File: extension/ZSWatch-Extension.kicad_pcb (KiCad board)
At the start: 4 copper layers, 16.8 x 16.8 mm, 37 parts, among them IC501 MAX32664, IC502 LIS2DS12, IC503 MAX86141, IC601 DA7212-01UM2, X701 MB2, X702 MB1, Y501 32kHz

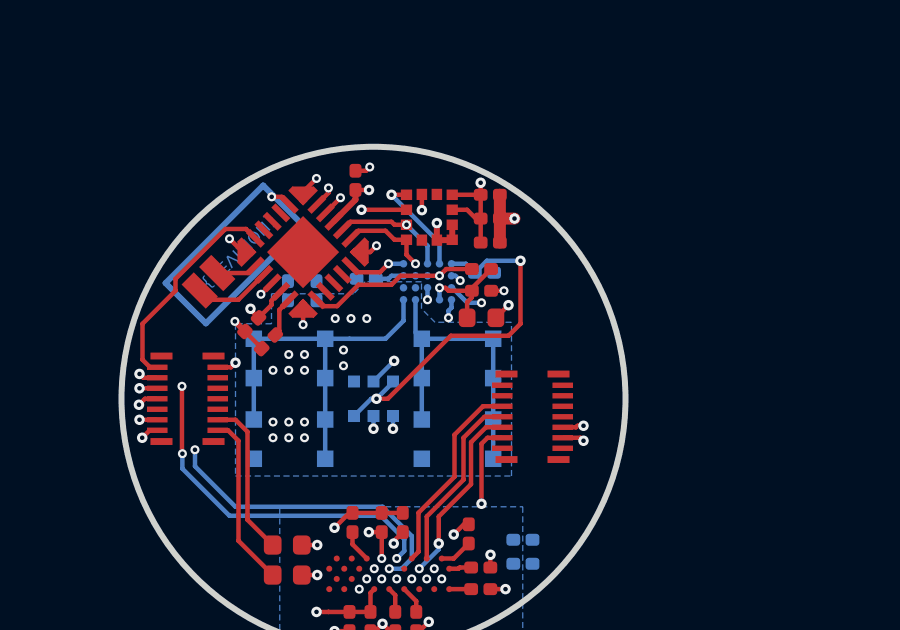
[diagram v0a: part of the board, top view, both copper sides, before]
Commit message: Bug: Issue #3
- Replace VLED capacitor with 10 V type

Closes: #3

Signed-off-by: Daniel Kampert <DanielKampert@kampis-elektroecke.de>
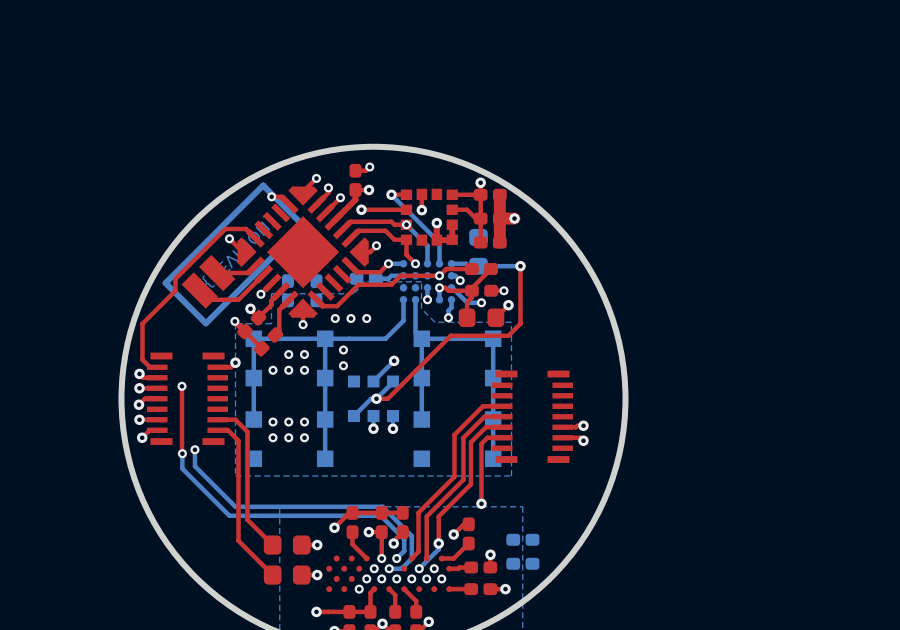
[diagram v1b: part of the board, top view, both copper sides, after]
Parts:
- C508: footprint Capacitor_SMD:C_0201_0603Metric -> Capacitor_SMD:C_0402_1005Metric
- moved C508 0.73 mm to (208.5, 145.1), turned to 90 degrees
